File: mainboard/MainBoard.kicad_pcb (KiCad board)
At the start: 2 copper layers, 121.5 x 73.2 mm, 172 parts, among them J1 CONN_1x4, J10 CONN_2X2, J11 CONN_2X2, J17 HV, J18 CONN_1X2, J19 CONN_1X2, J2 CONN_2X3, J3 CONN_2X3, J4 CONN_2X2, J5 SWDEBUG_CONNECTOR, J6 CONN_2X2, J7 CONN_2X12, J8 CONN_1X2, J9 Micro_SD_Card_Det_Hirose_DM3AT, K1 KT12-1A, K2 G6DN 12V, Q1 SSM3K361TU,LF, Q2 TSM2312, SW1 RESET, U1 VX07805-1000, U10 DCDC_ISO_5V_ISO, U11 STM32G474, U12 M95256-WMN6P, U13 TS3704IPT, U14 CD4044, U15 CD4082, U16 ADCMP350, U17 CD74HC4067SM, U19 TCMT1103, U2 TPS2115A, U23 CD4072BPW, U24 LM358, U26 TCMT1103, U27 DCDC_ISO_5V, U28 MIC5365-3.3YC5, U29 Si8900, U3 ld1117s33, U30 MAX14878AWA+, U4 MainBoard_AD8244, U5 MCP2562, U6 LM358, U7 ADCMP354, U8 LTC6820, U9 HM2103

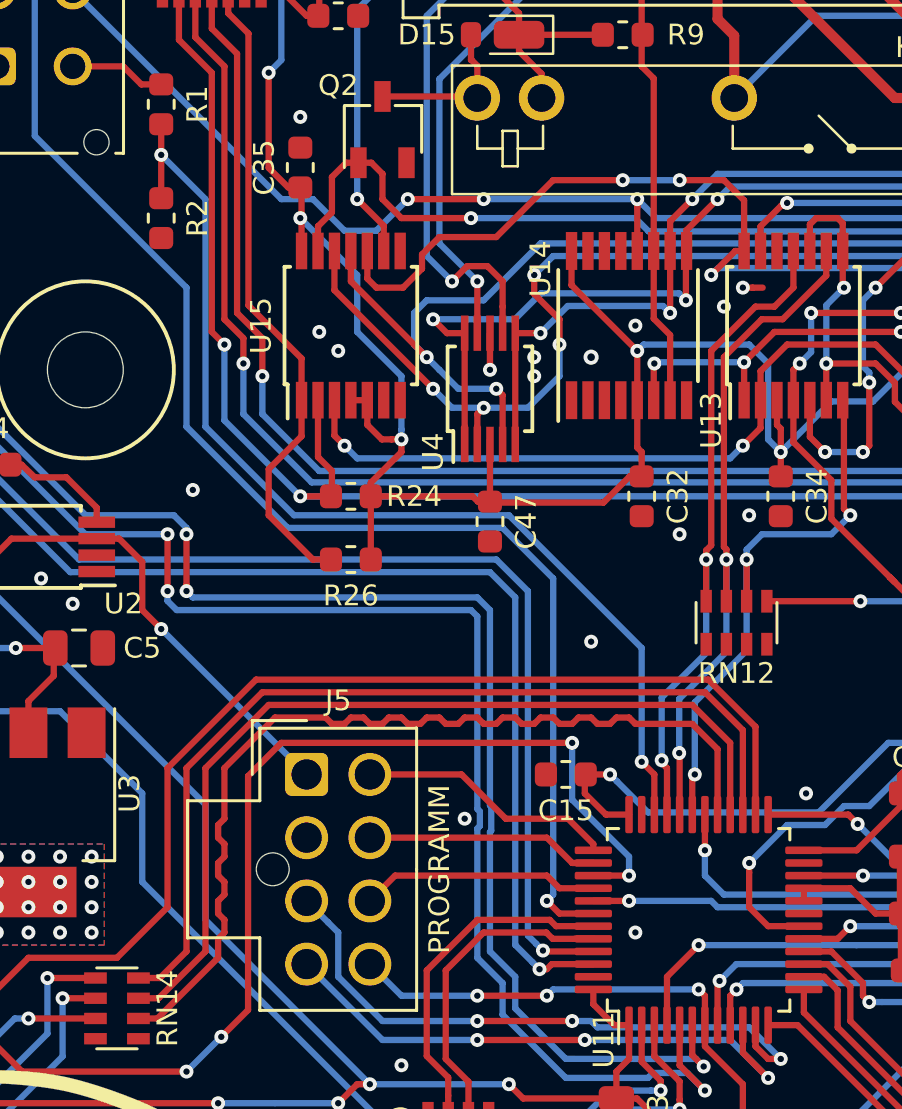
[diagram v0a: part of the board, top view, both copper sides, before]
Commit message: Corrected BOOT0
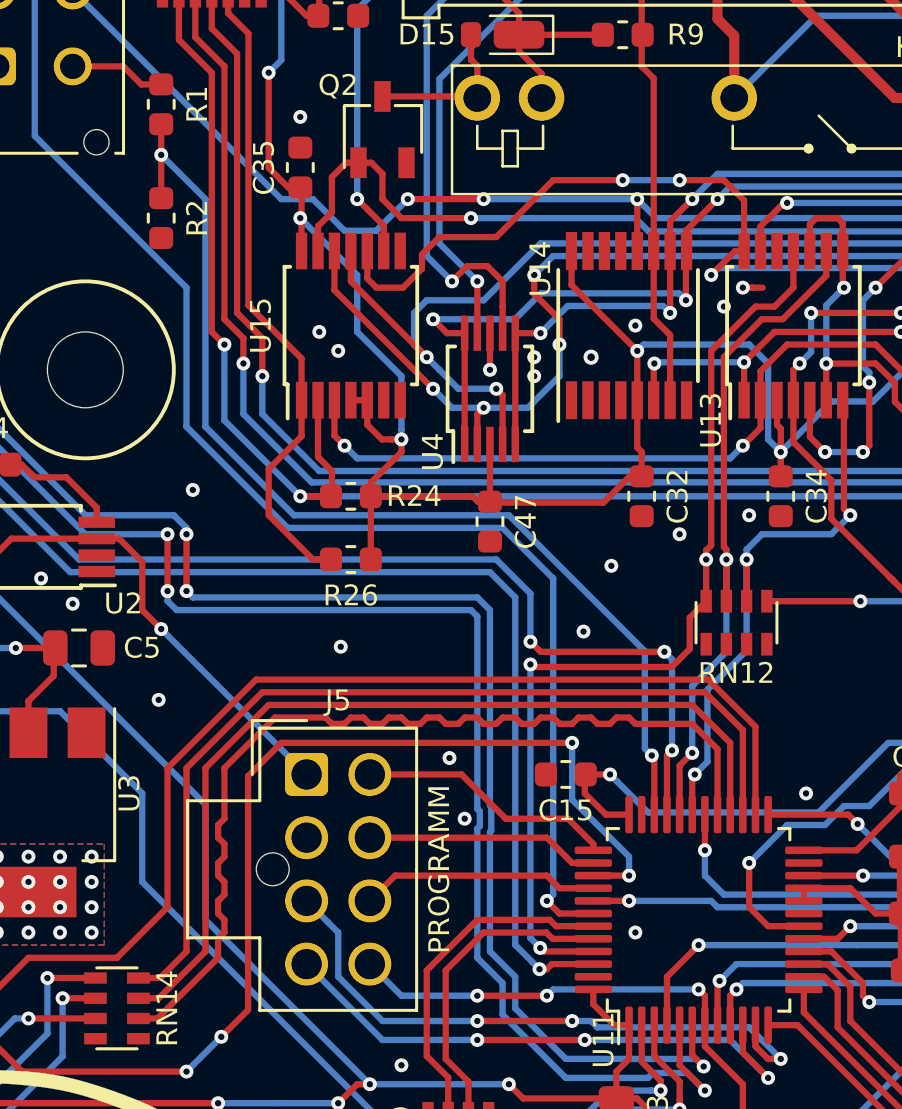
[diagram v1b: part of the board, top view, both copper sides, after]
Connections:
- RN10 pad 5: /AMS/A0 -> /AMS/A2
- RN10 pad 7: /AMS/A2 -> /AMS/A0
- U11 pad 33: /PC_ENDED -> /AMS/CAN_RX
- U11 pad 45: /AMS/CAN_RX -> /PC_ENDED
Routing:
- net /PC_ENDED: track 26.7 -> 38.0 mm, vias 2 -> 3
- net /AMS/CAN_RX: track 47.8 -> 45.5 mm, vias 2 -> 4
- net GND: vias 38 -> 42

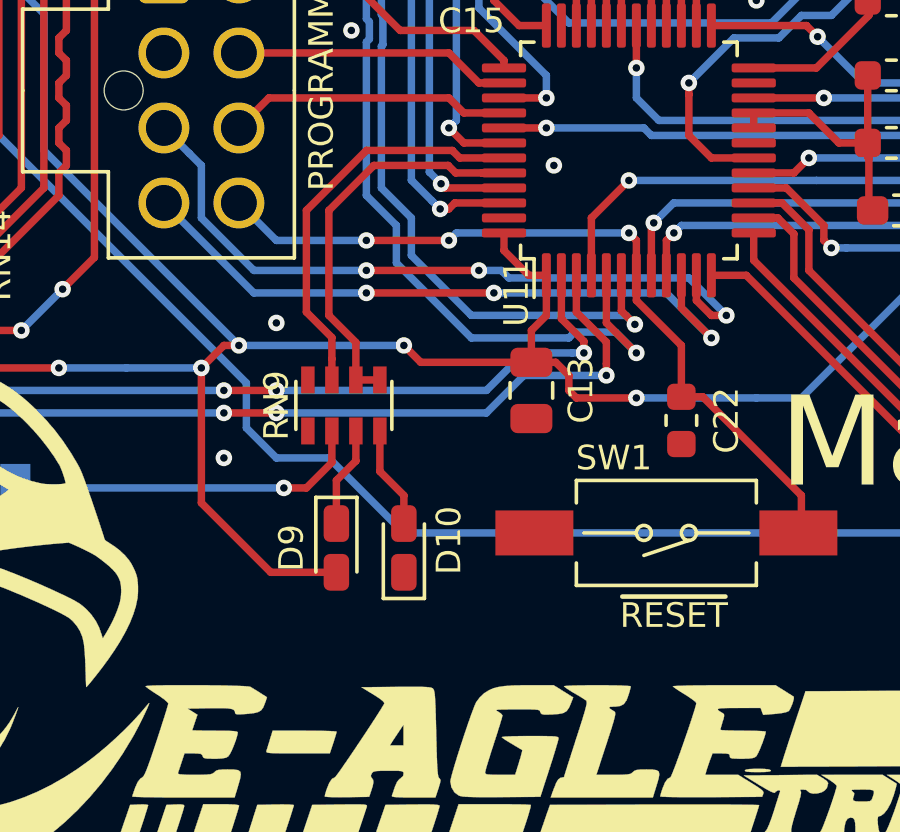
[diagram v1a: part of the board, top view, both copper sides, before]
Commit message: Added jumper for BOOT0 to 3V3
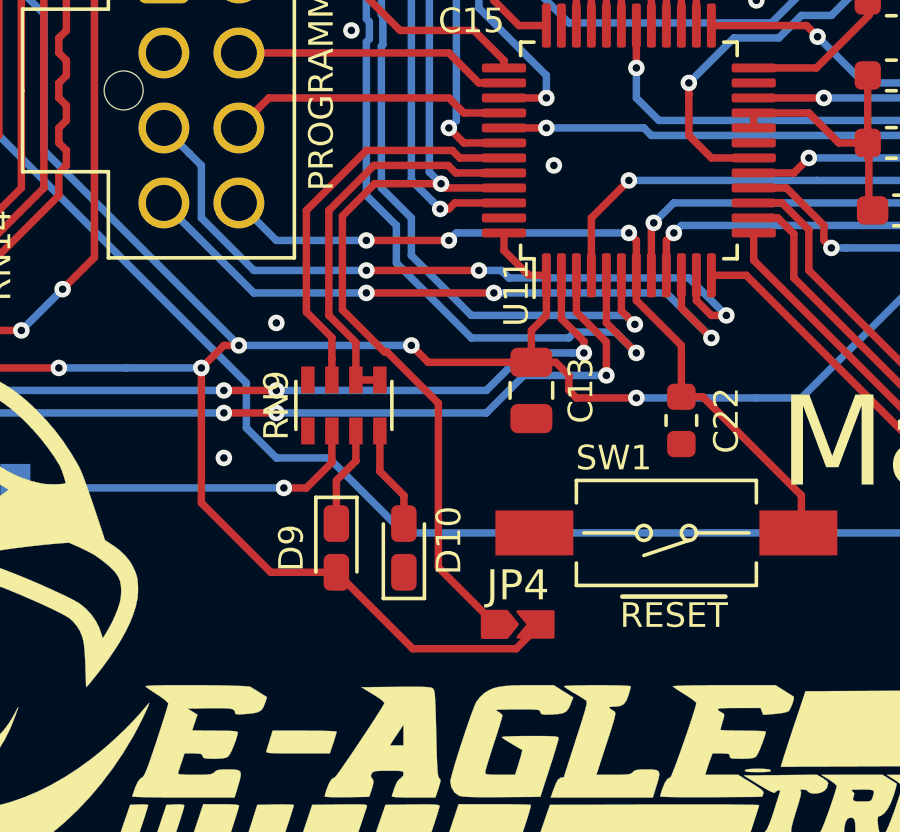
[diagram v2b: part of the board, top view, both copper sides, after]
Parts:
- added JP4: SolderJumper_2_Open, MainBoard:Jumper_SMD_0603, F.Cu at (68.5, 98.8)
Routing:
- net /PC_ENDED: track 38.0 -> 57.6 mm
- net +3V3: track 335.5 -> 343.7 mm

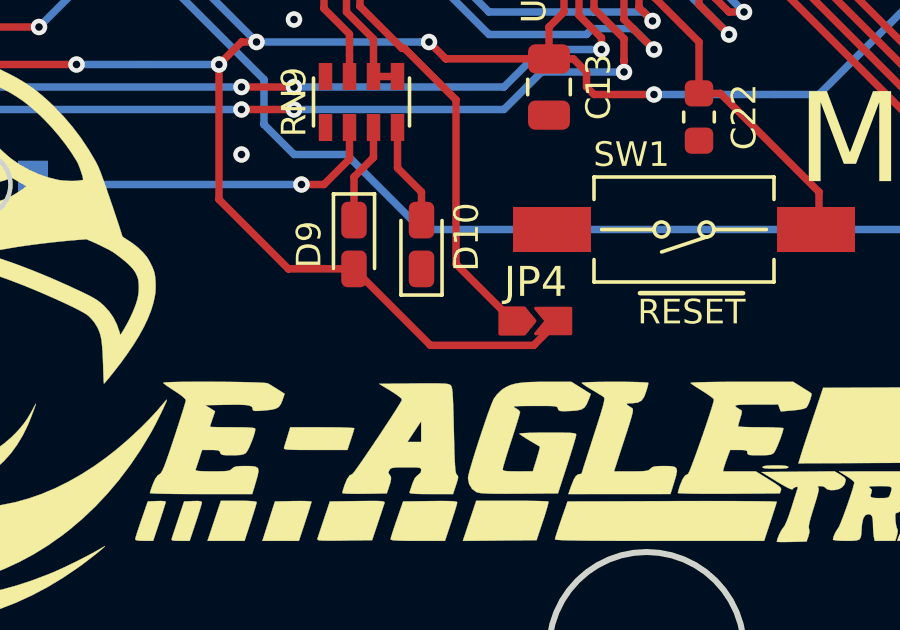
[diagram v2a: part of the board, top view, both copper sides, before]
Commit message: Added vias due to last boot0 modification
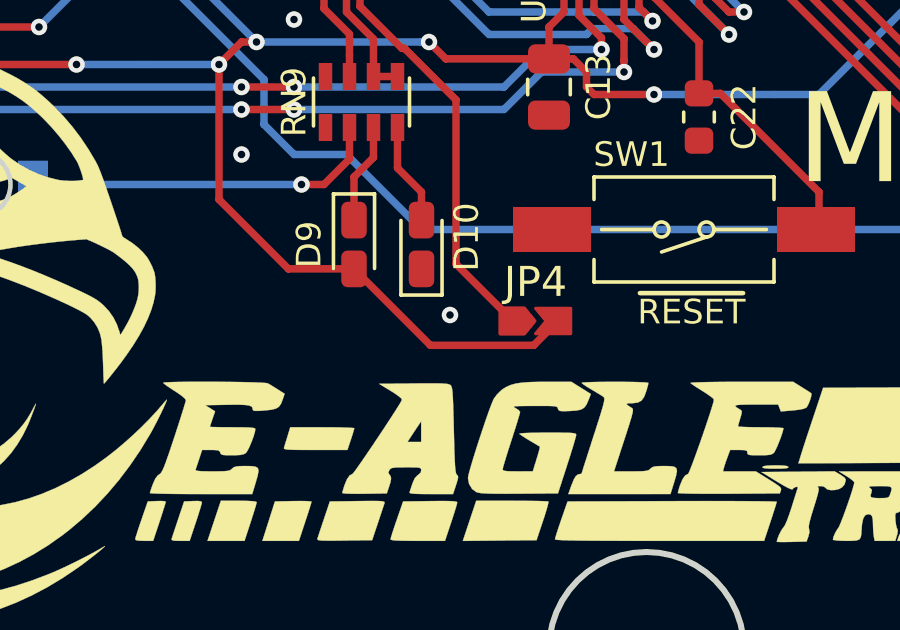
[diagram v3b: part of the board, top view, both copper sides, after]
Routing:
- net GND: vias 42 -> 43

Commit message: v1.1 as printed
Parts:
- removed C4, C5: 1uF, Capacitor_SMD:C_0805_2012Metric
- removed the G*** at (73.2, 103.5)
- removed the G*** at (44.8, 99.5)
- removed R38: 604, Resistor_SMD:R_0603_1608Metric
- removed R4: 470, Resistor_SMD:R_0603_1608Metric
- removed R69: 2K, Resistor_SMD:R_0603_1608Metric
- removed U10: DCDC_ISO_5V_ISO, MainBoard:DC_DC_ISO_ROExxxx
- removed U17: CD74HC4067SM, Package_SO:TSSOP-24_4.4x7.8mm_P0.65mm
- removed U23: CD4072BPW, Package_SO:TSSOP-14_4.4x5mm_P0.65mm
- removed U3: ld1117s33, Package_TO_SOT_SMD:SOT-223
- added B-H1: BOOT0, MainBoard:Jumper_SMD_0603, F.Cu at (131.8, 94.9)
- added C28: 1mF 16V, Capacitor_THT:CP_Radial_D10.0mm_P5.00mm, F.Cu at (167.0, 45.2)
- added C31: 100nF, Capacitor_SMD:C_0603_1608Metric, F.Cu at (187.0, 49.9)
- added C36: 1mF 16V, Capacitor_THT:CP_Radial_D10.0mm_P5.00mm, F.Cu at (167.0, 56.5)
- added C37: 100nF, Capacitor_SMD:C_0603_1608Metric, F.Cu at (187.0, 51.9)
- added C38: 20pF, Capacitor_SMD:C_0603_1608Metric, F.Cu at (164.3, 101.2)
- added C39: 20pF, Capacitor_SMD:C_0603_1608Metric, F.Cu at (164.2, 95.1)
- added C48: 100nF, Capacitor_SMD:C_0603_1608Metric, F.Cu at (157.7, 88.0)
- added D11: D, MainBoard:SOD_323HE, F.Cu at (196.1, 41.5)
- added D12: RGL34B, Diode_SMD:D_MiniMELF, F.Cu at (177.8, 45.2)
- added D13: DDZ13ASF 13V, Diode_SMD:D_SOD-323, F.Cu at (178.8, 41.3)
- added D16: D, MainBoard:SOD_323HE, F.Cu at (181.6, 55.1)
- added D17: D, MainBoard:SOD_323HE, F.Cu at (182.8, 46.5)
- added D18: RGL34B, Diode_SMD:D_MiniMELF, F.Cu at (177.8, 56.5)
- added D19: D, MainBoard:SOD_323HE, F.Cu at (218.1, 78.3)
- added D20: D, MainBoard:SOD_323HE, F.Cu at (218.1, 81.6)
- added D21: 1N4148W, Diode_SMD:D_SOD-123, F.Cu at (224.3, 100.0)
- added G***: LOGO, MainBoard:logo_21.2mm, F.Cu at (179.8, 102.2)
- added H5: MountingHole, MountingHole:MountingHole_3mm, F.Cu at (143.6, 56.0)
- added J12: SPARE_PINS, Connector_PinHeader_2.54mm:PinHeader_2x05_P2.54mm_Vertical, F.Cu at (154.2, 80.5)
- added JP1: prom_select, Jumper:SolderJumper-3_P1.3mm_Open_RoundedPad1.0x1.5mm, F.Cu at (213.7, 81.0)
- added JP2: 3V3_PROG, Jumper:SolderJumper-2_P1.3mm_Open_RoundedPad1.0x1.5mm, F.Cu at (122.5, 97.5)
- added JP5: AIR mode sel2, Jumper:SolderJumper-3_P1.3mm_Bridged12_RoundedPad1.0x1.5mm, F.Cu at (182.2, 62.1)
- added JP6: SolderJumper_3_Open, Jumper:SolderJumper-3_P1.3mm_Open_RoundedPad1.0x1.5mm, F.Cu at (230.2, 97.1)
- added JP7: SolderJumper_2_Open, Jumper:SolderJumper-2_P1.3mm_Open_RoundedPad1.0x1.5mm, F.Cu at (122.8, 50.0)
- added Q10: NTR5105PT1G, Package_TO_SOT_SMD:SOT-23, F.Cu at (131.7, 61.1)
- added Q11: NTR5105PT1G, Package_TO_SOT_SMD:SOT-23, F.Cu at (127.4, 61.1)
- added Q12: NTR5105PT1G, Package_TO_SOT_SMD:SOT-23, F.Cu at (123.1, 61.1)
- added Q3: DMN10H220L, Package_TO_SOT_SMD:SOT-23, F.Cu at (177.0, 51.4)
- added Q4: 2N7002NXAKR, Package_TO_SOT_SMD:SOT-23, F.Cu at (144.6, 65.7)
- added Q5: 2N7002NXAKR, Package_TO_SOT_SMD:SOT-23, F.Cu at (187.0, 60.8)
- added Q6: 2N7002NXAKR, Package_TO_SOT_SMD:SOT-23, F.Cu at (187.0, 46.8)
- added Q7: DMN10H220L, Package_TO_SOT_SMD:SOT-23, F.Cu at (177.0, 62.5)
- added Q8: NTR5105PT1G, Package_TO_SOT_SMD:SOT-23, F.Cu at (148.7, 65.7)
- added Q9: NTR5105PT1G, Package_TO_SOT_SMD:SOT-23, F.Cu at (152.7, 65.7)
- added R33: 0, Resistor_SMD:R_0603_1608Metric, F.Cu at (163.7, 48.1)
- added R36: 120, Resistor_SMD:R_0805_2012Metric, F.Cu at (209.0, 106.0)
- added R40: 0, Resistor_SMD:R_0603_1608Metric, F.Cu at (151.2, 70.1)
- added RN15: 100K, MainBoard:R_network_4x1_bourns_CAY16, F.Cu at (193.0, 50.9)
- added RN16: 330K, MainBoard:R_network_4x1_bourns_CAY16, F.Cu at (182.8, 50.9)
- added RN17: 100K, MainBoard:R_network_4x1_bourns_CAY16, F.Cu at (170.4, 79.8)
- added RN18: 100K, MainBoard:R_network_4x1_bourns_CAY16, F.Cu at (183.6, 91.2)
- added RN19: 22, MainBoard:R_network_4x1_bourns_CAY16, F.Cu at (191.4, 99.4)
- added RN20: 22, MainBoard:R_network_4x1_bourns_CAY16, F.Cu at (129.4, 65.8)
- added RN21: 22, MainBoard:R_network_4x1_bourns_CAY16, F.Cu at (148.7, 70.1)
- added RN22: 22, MainBoard:R_network_4x1_bourns_CAY16, F.Cu at (143.3, 100.8)
- added RV1: 10k, Potentiometer_SMD:Potentiometer_Bourns_3314J_Vertical, F.Cu at (226.1, 95.8)
- added SW2: SD_RESET, MainBoard:Button_SMD_6x3.5x4.3mm, F.Cu at (120.2, 79.5)
- added TP1: 3V3, TestPoint:TestPoint_Pad_D1.0mm, F.Cu at (125.6, 97.1)
- added TP10: TS_DIVIDER, TestPoint:TestPoint_Pad_D1.0mm, F.Cu at (223.8, 66.2)
- added TP11: 5VISO, TestPoint:TestPoint_Pad_D1.0mm, F.Cu at (216.2, 98.6)
- added TP12: TSV_FT, TestPoint:TestPoint_Pad_D1.0mm, F.Cu at (213.5, 88.8)
- added TP13: PackV_FT, TestPoint:TestPoint_Pad_D1.0mm, F.Cu at (213.5, 86.6)
- added TP14: 3V3ISO, TestPoint:TestPoint_Pad_D1.0mm, F.Cu at (216.3, 92.0)
- added TP15: Ip_high, TestPoint:TestPoint_Pad_D1.0mm, F.Cu at (106.0, 57.0)
- added TP16: BMS_FAULT, TestPoint:TestPoint_Pad_D1.0mm, F.Cu at (138.6, 83.9)
- added TP17: MUX_OUTPUT, TestPoint:TestPoint_Pad_D1.0mm, F.Cu at (155.8, 86.8)
- added TP18: TS_OVER_60V, TestPoint:TestPoint_Pad_D1.0mm, F.Cu at (194.1, 67.6)
- added TP19: PC_ST, TestPoint:TestPoint_Pad_D1.0mm, F.Cu at (134.2, 65.8)
- added TP2: 5V, TestPoint:TestPoint_Pad_D1.0mm, F.Cu at (116.0, 98.5)
- added TP20: AIR+_GATE, TestPoint:TestPoint_Pad_D1.0mm, F.Cu at (190.2, 48.0)
- added TP21: AIR-_GATE, TestPoint:TestPoint_Pad_D1.0mm, F.Cu at (190.2, 46.0)
- added TP22: AIR+_STATUS, TestPoint:TestPoint_Pad_D1.0mm, F.Cu at (163.2, 62.1)
- added TP23: AIR-_STATUS, TestPoint:TestPoint_Pad_D1.0mm, F.Cu at (161.4, 64.0)
- added TP24: SD_OK, TestPoint:TestPoint_Pad_D1.0mm, F.Cu at (136.3, 65.8)
- added TP25: BMS_LATCHED, TestPoint:TestPoint_Pad_D1.0mm, F.Cu at (125.0, 65.6)
- added TP26: IMD_LATCHED, TestPoint:TestPoint_Pad_D1.0mm, F.Cu at (125.0, 67.6)
- added TP27: TS_ON, TestPoint:TestPoint_Pad_D1.0mm, F.Cu at (140.7, 83.9)
- added TP28: TS_ON_12V, TestPoint:TestPoint_Pad_D1.0mm, F.Cu at (138.3, 65.8)
- added TP29: GND, MainBoard:TestPoint_GNDedge, F.Cu at (106.2, 110.8)
- added TP3: 12V, TestPoint:TestPoint_Pad_D1.0mm, F.Cu at (90.4, 85.1)
- added TP30: GND, MainBoard:TestPoint_GNDedge, F.Cu at (186.6, 39.7)
- added TP31: -BATT, MainBoard:TestPoint_GNDedge, F.Cu at (207.3, 110.8)
- added TP33: VCAP, TestPoint:TestPoint_Pad_D1.0mm, F.Cu at (150.5, 82.6)
- added TP35: IMD_PWM, TestPoint:TestPoint_Pad_D1.0mm, F.Cu at (114.4, 57.8)
- added TP38: VS_FT, TestPoint:TestPoint_Pad_D1.0mm, F.Cu at (213.5, 84.4)
- added TP4: FROM_SD, TestPoint:TestPoint_Pad_D1.0mm, F.Cu at (182.7, 70.0)
- added TP43: 11, TestPoint:TestPoint_Pad_D1.0mm, F.Cu at (196.1, 58.1)
- added TP44: 9, TestPoint:TestPoint_Pad_D1.0mm, F.Cu at (195.7, 60.2)
- added TP45: 13, TestPoint:TestPoint_Pad_D1.0mm, F.Cu at (196.3, 55.7)
- added TP46: 14, TestPoint:TestPoint_Pad_D1.0mm, F.Cu at (196.5, 53.5)
- added TP5: FROM_TSMS, TestPoint:TestPoint_Pad_D1.0mm, F.Cu at (182.7, 66.0)
- added TP6: TO_TSMS, TestPoint:TestPoint_Pad_D1.0mm, F.Cu at (182.7, 68.0)
- added TP7: BSPD_SIG, TestPoint:TestPoint_Pad_D1.0mm, F.Cu at (140.4, 65.9)
- added TP8: IMD_FAULT, TestPoint:TestPoint_Pad_D1.0mm, F.Cu at (116.9, 48.6)
- added TP9: Ip_low, TestPoint:TestPoint_Pad_D1.0mm, F.Cu at (106.0, 55.1)
- added Y1: 26MHz, Crystal:Crystal_SMD_3225-4Pin_3.2x2.5mm, F.Cu at (164.3, 98.2)
- C1: value 22uF -> 100nF; footprint Capacitor_SMD:C_1206_3216Metric -> Capacitor_SMD:C_0603_1608Metric
- C19, C21: value 100nF -> 1uF; footprint Capacitor_SMD:C_0603_1608Metric -> Capacitor_SMD:C_0805_2012Metric
- C2: value 10uF -> 100nF; footprint Capacitor_SMD:C_0805_2012Metric -> Capacitor_SMD:C_0603_1608Metric
- C25: footprint Capacitor_SMD:C_0603_1608Metric -> Capacitor_SMD:C_0805_2012Metric
- C3: value 1uF -> 100nF; footprint Capacitor_SMD:C_0805_2012Metric -> Capacitor_SMD:C_0603_1608Metric
- C42: value 6.8uF -> 10uF
- D14: value 12V -> DDZ13ASF 13V
- D5, D6, D7: value 3V -> DDZ3V3ASF 3V3
- J10: value CONN_2X2 -> AIR+
- J4: footprint MainBoard:Molex_Micro-Fit_3.0_43045-0412_2x02_P3.00mm_Vertical -> MainBoard:Molex_Micro-Fit_3.0_43045-0612_2x03_P3.00mm_Vertical
- J5: footprint MainBoard:Molex_Nano-Fit_105310-xx08_2x04_P2.50mm_Vertical -> Connector_Molex:Molex_Nano-Fit_105310-xx10_2x05_P2.50mm_Vertical
- J6: value CONN_2X2 -> AIR-
- J9: footprint MainBoard:MicroSD_Hirose_DM3AT-SF-PEJM5 -> Connector_Card:microSD_HC_Hirose_DM3AT-SF-PEJM5
- JP3: footprint MainBoard:Jumper_SMD_0603 -> Jumper:SolderJumper-2_P1.3mm_Open_RoundedPad1.0x1.5mm
- JP4: value SolderJumper_2_Open -> AIR mode sel1; footprint MainBoard:Jumper_SMD_0603 -> Jumper:SolderJumper-3_P1.3mm_Bridged12_RoundedPad1.0x1.5mm
- Q1: value SSM3K361TU,LF -> NTR5105PT1G; footprint Package_TO_SOT_SMD:SOT-323_SC-70 -> Package_TO_SOT_SMD:SOT-23
- Q2: value TSM2312 -> DMN10H220L; footprint Package_TO_SOT_SMD:TSOT-23 -> Package_TO_SOT_SMD:SOT-23
- R13: value 330K -> 1M
- R16: value 1M -> 1K
- R19: value 2K -> 1K
- R20: value 2K -> 0
- R30: value 100K -> 0
- R31, R32: value 22 -> 0
- R34: value 150 -> 0
- R35: value 150 -> 120; footprint Resistor_SMD:R_0603_1608Metric -> Resistor_SMD:R_0805_2012Metric
- R39: value 1K4 -> 0
- R56, R64, R66: footprint Resistor_SMD:R_1206_3216Metric -> Resistor_SMD:R_2010_5025Metric
- R59: value 1K -> 100
- R6: value 120 -> 10K; footprint Resistor_SMD:R_0805_2012Metric -> Resistor_SMD:R_0603_1608Metric
- RN1: value 1K -> 100K
- RN5: value 100K -> 330K
- U1: value VX07805-1000 -> Tex_DCDC; footprint MainBoard:DC_DC_VXO7805_1000 -> MainBoard:Tex_DCDC_vertical
- U11: value STM32G474 -> TS3704IPT; footprint Package_QFP:LQFP-48_7x7mm_P0.5mm -> Package_SO:TSSOP-14_4.4x5mm_P0.65mm
- U2: value TPS2115A -> TSC211; footprint Package_SO:TSSOP-8_4.4x3mm_P0.65mm -> Package_TO_SOT_SMD:SOT-363_SC-70-6
- U30: footprint Package_SO:SOIC-8_7.5x5.85mm_P1.27mm -> Package_SO:SOIC-8W_5.3x5.3mm_P1.27mm
- U4: moved to B.Cu
- U8: value LTC6820 -> CD74HC4067SM; footprint MainBoard:MSOP-16 -> Package_SO:TSSOP-24_4.4x7.8mm_P0.65mm
- U9: value HM2103 -> STM32F446RE_64PIN; footprint MainBoard:HM2103 -> Package_QFP:LQFP-64_10x10mm_P0.5mm
- moved C1 201.1 mm to (225.2, 101.8), turned to 180 degrees
- moved C2 192.3 mm to (225.2, 103.5), turned to 0 degrees
- moved U2 186.0 mm to (228.2, 102.8), turned to 0 degrees
- moved R19 180.4 mm to (209.9, 77.5)
- moved R3 176.9 mm to (215.3, 84.4), turned to 0 degrees
- moved C3 169.2 mm to (211.8, 84.4), turned to 180 degrees
- moved R24 138.0 mm to (196.5, 68.8), turned to 270 degrees
- moved D8 134.8 mm to (184.8, 97.1), turned to 180 degrees
- moved U11 121.2 mm to (190.4, 56.3), turned to 0 degrees
- moved JP4 120.3 mm to (182.2, 59.4), turned to 0 degrees
- moved R16 112.2 mm to (211.5, 77.5), turned to 270 degrees
- moved J8 109.8 mm to (232.1, 104.6)
- moved C29 105.5 mm to (190.7, 59.9), turned to 0 degrees
- moved J19 100.0 mm to (239.1, 93.1), turned to 90 degrees
- moved J18 99.9 mm to (239.2, 104.7), turned to 90 degrees
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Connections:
- net /HV/5V_FROM_CELL renamed Net-(C17-Pad1)
- net /Shutdown/dissipation renamed /AIRs/dissipation
- C1 pad 1: +12V -> /HV/0V5ref
- C1 pad 2: GND -> -BATT
- C18 pad 1: +5V -> +3V3
- C19 pad 1: GND -> Net-(C19-Pad1)
- C19 pad 2: Net-(C19-Pad2) -> GND
- C2 pad 1: /5V_FROM_12V -> -BATT
- C2 pad 2: GND -> /HV/3V3ISO
- C21 pad 1: +3V3 -> Net-(C19-Pad1)
- C29 pad 1: +3V3 -> +12V
- C3 pad 1: /5V_USB -> -BATT
- C3 pad 2: GND -> /HV/VS_FT
- F2 pad 1: Net-(C5-Pad1) -> /3V3_prefuse
- J10 pad 1: /FROM_TSMS -> /AIRs/AIR+_STATUS
- J10 pad 2: /Shutdown/LAST_AIR -> +12V
- J10 pad 3: /FB_AIR+ -> Net-(J10-Pad3)
- J10 pad 4: +12V -> Net-(C36-Pad1)
- J11 pad 1: /IM -> /HV/ISO_CANL
- J11 pad 2: /IP -> /HV/ISO_CANH
- J3 pad 5: /IMD_Fault -> /IMD_FAULT
- J4 pad 1: /HV/EXT_GND -> /HV/PROMINENT-
- J4 pad 2: /HV/PROMINENT- -> /HV/PROMINENT+
- J4 pad 3: /HV/EXT_5V -> /HV/JUMPER_CELLBOARD
- J4 pad 4: /HV/PROMINENT+ -> /HV/CELLBOARD_5V
- J5 pad 1: /5V_USB -> GND
- J5 pad 2: GND -> /SWCLK_MCU
- J5 pad 3: /RX_MCU -> /SWDIO_MCU
- J5 pad 4: /TX_MCU -> Net-(J5-Pad4)
- J5 pad 5: /SWDIO_MCU -> /TX_MCU
- J5 pad 6: /SWCLK_MCU -> GND
- J5 pad 7: /SWO_MCU -> /NRST_MCU
- J5 pad 8: /NRST_MCU -> /SWO_MCU
- J6 pad 1: +12V -> /AIRs/AIR-_STATUS
- J6 pad 2: /FB_AIR- -> +12V
- J6 pad 3: GND -> Net-(J6-Pad3)
- J6 pad 4: /FROM_TSMS -> Net-(C28-Pad1)
- J7 pad 7: /LED_INDICATOR -> /TSAL
- J8 pad 1: /IP -> /HV/VS-
- J8 pad 2: /IM -> /HV/VS+
- JP4 pad 1: +3V3 -> Net-(D16-Pad1)
- JP4 pad 2: /PC_ENDED -> Net-(JP4-Pad2)
- Q1 pad 1: /FB_PC_END -> Net-(Q1-Pad1)
- Q1 pad 2: GND -> +12V
- Q1 pad 3: /Shutdown/LAST_AIR -> Net-(Q1-Pad3)
- Q2 pad 1: /FB_SD_MINIRELAY -> Net-(Q2-Pad1)
- R1 pad 2: /IMD -> /IMD_PWM
- R13 pad 1: +3V3 -> Net-(D5-Pad1)
- R13 pad 2: /AMS/MISO -> /FROM_SD
- R14 pad 1: Net-(D5-Pad1) -> Net-(D6-Pad1)
- R14 pad 2: /FROM_SD -> /TO_TSMS
- R15 pad 1: Net-(D6-Pad1) -> Net-(D7-Pad1)
- R15 pad 2: /TO_TSMS -> /FROM_TSMS
- R16 pad 1: Net-(D7-Pad1) -> Net-(R16-Pad1)
- R16 pad 2: /FROM_TSMS -> /HV/3V3ISO
- R19 pad 1: +3V3 -> /HV/~RST~_8902
- R19 pad 2: /AMS/~W~ -> Net-(R16-Pad1)
- R2 pad 1: /IMD -> /IMD_PWM
- R20 pad 1: +3V3 -> Net-(D4-Pad1)
- R20 pad 2: /AMS/MISO_2 -> /TSAL
- R24 pad 2: /FB_TS_OVER_60V -> /Probing/FB_OVER_60V_12V
- R25 pad 1: /BSPD_SIG -> GND
- R25 pad 2: GND -> /BSPD_SIG
- R27 pad 1: GND -> Net-(D4-Pad2)
- R27 pad 2: Net-(D4-Pad1) -> +12V
- R3 pad 1: /5V_USB -> /HV/VS_FT
- R3 pad 2: GND -> /HV/VS
- R30 pad 1: /AMS/CHECK_MUX -> /FROM_TSMS
- R30 pad 2: +3V3 -> Net-(C36-Pad1)
- R31 pad 1: /AMS/ADC_TX -> /FROM_TSMS
- R31 pad 2: Net-(R31-Pad2) -> Net-(C28-Pad1)
- R32 pad 1: /AMS/ADC_RX -> GND
- R32 pad 2: Net-(R32-Pad2) -> Net-(J10-Pad3)
- R34 pad 1: /AMS/IP_LV -> Net-(Q1-Pad3)
- R34 pad 2: Net-(C19-Pad2) -> /TSAL
- R35 pad 1: Net-(C19-Pad2) -> /CAN+
- R35 pad 2: /AMS/IM_LV -> /CAN-
- R39 pad 1: GND -> /Shutdown/EN_BMS_SD
- R39 pad 2: /AMS/ICMP -> /Shutdown/BMS_LATCHED
- R6 pad 1: /IP -> +3V3
- R6 pad 2: /IM -> /AMS/SPI2_MISO
- RN1 pad 2: Net-(RN1-Pad2) -> +3V3
- RN1 pad 7: Net-(RN1-Pad7) -> /AMS/~W~
- RN10 pad 5: /AMS/A2 -> /Probing/FB_AIR+_GATE
- RN10 pad 6: /AMS/A1 -> /Probing/FB_AIR-
- RN10 pad 7: /AMS/A0 -> /Probing/FB_AIR+
- RN10 pad 8: /AMS/A3 -> /Probing/FB_LATCH_BMS
- RN11 pad 1: /AMS/FB_PC_END_12V -> GND
- RN11 pad 2: /AMS/FB_AIR- -> GND
- RN11 pad 3: /AMS/FB_AIR+ -> GND
- RN11 pad 4: /AMS/FB_TSAL_OVER60V -> GND
- RN11 pad 5: GND -> /Probing/FB_LATCH_IMD
- RN11 pad 6: GND -> /Probing/FB_BMS_SD
- RN11 pad 7: GND -> /Probing/FB_IMD_SD
- RN11 pad 8: GND -> /Probing/FB_BMS_12V
- RN12 pad 5: /PC_ENDED -> /AMS/BOOT0
- RN12 pad 6: /TS_ON -> /AMS/TS_ON
- RN12 pad 7: /BMS_Fault -> /AMS/BMS_FAULT
- RN14 pad 1: /AMS/SPI2_SCK -> Net-(RN14-Pad1)
- RN14 pad 2: /AMS/SPI2_MISO -> /AMS/SPI2_MOSI
- RN14 pad 3: /AMS/SPI2_MOSI -> /AMS/SPI2_SCK
- RN14 pad 4: Net-(RN14-Pad4) -> /AMS/SPI2_MISO
- RN14 pad 5: Net-(RN14-Pad5) -> /AMS/MISO_2
- RN14 pad 6: /AMS/MOSI_2 -> /AMS/SCK_2
- RN14 pad 7: /AMS/MISO_2 -> /AMS/MOSI_2
- RN14 pad 8: /AMS/SCK_2 -> Net-(RN14-Pad8)
- RN2 pad 1: /FB_BMS -> /AIRs/AIR-_GATE
- RN2 pad 2: /IMD_Fault -> +3V3
- RN2 pad 3: /FB_LACTH_BMS -> /Probing/FB_RELAY_LV_12V
- RN2 pad 4: /FB_LACTH_IMD -> /IMD_FAULT
- RN2 pad 5: /AMS/FB_LATCH_IMD -> /AMS/FB_IMD_FAULT
- RN2 pad 6: /AMS/FB_LATCH_BMS -> /AMS/FB_RELAY_LV
- RN2 pad 7: /AMS/FB_IMD_FAULT -> /Probing/CHECK_MUX
- RN2 pad 8: /AMS/FB_BMS_12V -> /Probing/FB_AIR-_GATE
- RN3 pad 1: /FB_TS_ON -> /AIRs/AIR+_GATE
- RN3 pad 2: /FB_BMS_SD -> /TSAL
- RN3 pad 3: /FB_IMD_SD -> /Shutdown/BMS_LATCHED
- RN3 pad 4: /FB_SD_MINIRELAY -> /Probing/FB_LATCH_IMD_12V
- RN3 pad 5: /AMS/FB_RELAY_LV -> /Probing/FB_LATCH_BMS
- RN3 pad 6: /AMS/FB_IMD_SD -> /Probing/FB_AIR+
- RN3 pad 7: /AMS/FB_BMS_SD -> /Probing/FB_AIR-
- RN3 pad 8: /AMS/FB_TS_ON_12V -> /Probing/FB_AIR+_GATE
- RN4 pad 1: /FB_PC_END -> /Probing/FB_TS_ON_TO_12V
- RN4 pad 2: /FB_AIR- -> /Shutdown/EN_BMS_SD
- RN4 pad 3: /FB_AIR+ -> /Shutdown/EN_IMD_SD
- RN4 pad 4: /FB_TS_OVER_60V -> /Shutdown/BMS_FAULT_12V
- RN4 pad 5: /AMS/FB_TSAL_OVER60V -> /Probing/FB_BMS_12V
- RN4 pad 6: /AMS/FB_AIR+ -> /Probing/FB_IMD_SD
- RN4 pad 7: /AMS/FB_AIR- -> /Probing/FB_BMS_SD
- RN4 pad 8: /AMS/FB_PC_END_12V -> /Probing/FB_LATCH_IMD
- RN5 pad 1: /AMS/FB_BMS_12V -> /BSPD_SIG
- RN5 pad 2: /AMS/FB_IMD_FAULT -> /AIRs/AIR-_STATUS
- RN5 pad 3: /AMS/FB_LATCH_BMS -> /AIRs/AIR+_STATUS
- RN5 pad 4: /AMS/FB_LATCH_IMD -> /Probing/FB_OVER_60V_12V
- RN5 pad 5: GND -> /Probing/FB_TSAL_OVER60V
- RN5 pad 6: GND -> /Probing/FB_TSAL
- RN5 pad 7: GND -> /Probing/FB_BSPD_SIG
- RN5 pad 8: GND -> /Probing/FB_TS_ON_12V
- RN6 pad 1: /AMS/FB_TS_ON_12V -> Net-(RN6-Pad1)
- RN6 pad 2: /AMS/FB_BMS_SD -> /AMS/FB_FROM_TSMS
- RN6 pad 3: /AMS/FB_IMD_SD -> /Probing/FB_TO_TSMS
- RN6 pad 4: /AMS/FB_RELAY_LV -> /Probing/FB_FROM_SD
- RN6 pad 5: GND -> Net-(D5-Pad1)
- RN6 pad 6: GND -> Net-(D6-Pad1)
- RN6 pad 7: GND -> Net-(D7-Pad1)
- RN6 pad 8: GND -> Net-(RN6-Pad8)
- RN7 pad 1: Net-(D5-Pad1) -> GND
- RN7 pad 2: Net-(D6-Pad1) -> GND
- RN7 pad 3: Net-(D7-Pad1) -> GND
- RN7 pad 4: Net-(RN7-Pad4) -> GND
- RN7 pad 5: Net-(RN7-Pad5) -> /Probing/FB_AIR-_GATE
- RN7 pad 6: /AMS/FB_FROM_TSMS -> /Probing/CHECK_MUX
- RN7 pad 7: /AMS/FB_TO_TSMS -> /AMS/FB_RELAY_LV
- RN7 pad 8: /AMS/FB_FROM_SD -> /AMS/FB_IMD_FAULT
- RN8 pad 2: /LED_INDICATOR -> /TSAL
- RN8 pad 5: +12V -> GND
- RN8 pad 6: +12V -> GND
- RN8 pad 7: +12V -> GND
- U1 pad 1: +12V -> /3V3_prefuse
- U1 pad 3: /5V_FROM_12V -> Net-(F1-Pad2)
- U11 pad 1: +3V3 -> /AIRs/AIR-_GATE
- U11 pad 10: /TX_MCU -> +3V3
- U11 pad 11: /RX_MCU -> Net-(TP43-Pad1)
- U11 pad 12: /AMS/CS_6820 -> GND
- U11 pad 13: /AMS/SCK -> Net-(TP45-Pad1)
- U11 pad 14: /AMS/MISO -> Net-(TP46-Pad1)
- U11 pad 2: /AMS/CS_EEPROM -> /AIRs/AIR+_GATE
- U11 pad 3: /AMS/CARD_OK -> +12V
- U11 pad 4: /AMS/A1 -> Net-(JP5-Pad2)
- U11 pad 5: /AMS/Ip_low -> Net-(C37-Pad1)
- U11 pad 6: /AMS/Ip_high -> +3V3
- U11 pad 7: /NRST_MCU -> Net-(C31-Pad1)
- U11 pad 8: /AMS/A0 -> +3V3
- U11 pad 9: /AMS/A3 -> Net-(TP44-Pad1)
- U13 pad 1: /FB_BMS -> /Shutdown/BMS_FAULT_12V
- U13 pad 11: /PC_ENDED -> Net-(U13-Pad11)
- U13 pad 13: /FB_PC_END -> Net-(U13-Pad13)
- U13 pad 14: /FB_TS_ON -> /Probing/FB_TS_ON_TO_12V
- U13 pad 7: /BMS_Fault -> /AMS/BMS_FAULT
- U13 pad 9: /TS_ON -> /AMS/TS_ON
- U14 pad 10: /FB_LACTH_IMD -> /Probing/FB_LATCH_IMD_12V
- U14 pad 12: /IMD_Fault -> /IMD_FAULT
- U14 pad 6: /FB_BMS -> /Shutdown/BMS_FAULT_12V
- U14 pad 9: /FB_LACTH_BMS -> /Shutdown/BMS_LATCHED
- U15 pad 10: /FB_TS_ON -> /Probing/FB_TS_ON_TO_12V
- U15 pad 11: /FB_IMD_SD -> /Shutdown/EN_IMD_SD
- U15 pad 12: /FB_BMS_SD -> /Shutdown/EN_BMS_SD
- U15 pad 13: /FB_SD_MINIRELAY -> /Probing/FB_RELAY_LV_12V
- U15 pad 2: /FB_TS_OVER_60V -> /Probing/FB_OVER_60V_12V
- U19 pad 4: /FB_TS_OVER_60V -> /Probing/FB_OVER_60V_12V
- U2 pad 1: Net-(U2-Pad1) -> /HV/0V5ref
- U2 pad 2: GND -> -BATT
- U2 pad 3: /5V_USB -> /HV/3V3ISO
- U2 pad 4: Net-(R4-Pad2) -> /HV/VS+
- U2 pad 5: GND -> /HV/VS-
- U2 pad 6: /5V_FROM_12V -> /HV/VS
- U29 pad 12: Net-(R32-Pad2) -> Net-(RN19-Pad1)
- U29 pad 13: Net-(R31-Pad2) -> Net-(RN19-Pad2)
- U29 pad 5: Net-(U29-Pad5) -> /HV/VS_FT
- U30 pad 1: /AMS/ISO_CAN_RX -> Net-(RN19-Pad3)
- U30 pad 2: /AMS/ISO_CAN_TX -> Net-(RN19-Pad4)
- U30 pad 6: /IM -> /HV/ISO_CANL
- U30 pad 7: /IP -> /HV/ISO_CANH
- U4 pad 1: /FB_LACTH_BMS -> /Shutdown/BMS_LATCHED
- U4 pad 10: /FB_LACTH_BMS -> /Shutdown/BMS_LATCHED
- U4 pad 2: /FB_BMS_SD -> /Shutdown/EN_BMS_SD
- U4 pad 4: /FB_IMD_SD -> /Shutdown/EN_IMD_SD
- U4 pad 5: /FB_LACTH_IMD -> /Probing/FB_LATCH_IMD_12V
- U4 pad 6: /FB_LACTH_IMD -> /Probing/FB_LATCH_IMD_12V
- U5 pad 1: /AMS/CAN_TX -> Net-(RN22-Pad3)
- U5 pad 4: /AMS/CAN_RX -> Net-(RN22-Pad4)
- U8 pad 1: GND -> /AMS/MUX_OUTPUT
- U8 pad 10: /AMS/IM_LV -> /AMS/MUX_A0
- U8 pad 11: /AMS/IP_LV -> /AMS/MUX_A1
- U8 pad 12: +5V -> GND
- U8 pad 13: GND -> /AMS/MUX_A3
- U8 pad 14: GND -> /AMS/MUX_A2
- U8 pad 15: /AMS/ICMP -> GND
- U8 pad 16: /AMS/IBIAS -> /Probing/FB_TO_TSMS
- U8 pad 2: /AMS/MOSI -> /Probing/FB_BMS_12V
- U8 pad 3: /AMS/MISO -> /Probing/FB_IMD_SD
- U8 pad 4: /AMS/SCK -> /Probing/FB_BMS_SD
- U8 pad 5: /AMS/CS_6820 -> /Probing/FB_LATCH_IMD
- U8 pad 6: +3V3 -> /Probing/FB_TSAL_OVER60V
- U8 pad 7: GND -> /Probing/FB_TSAL
- U8 pad 8: GND -> /Probing/FB_BSPD_SIG
- U8 pad 9: +5V -> /Probing/FB_TS_ON_12V
- U9 pad 1: /IM -> +3V3
- U9 pad 2: Net-(U9-Pad2) -> /AMS/PC13
- U9 pad 3: /IP -> Net-(U9-Pad3)
- U9 pad 4: /AMS/IP_LV -> Net-(U9-Pad4)
- U9 pad 6: /AMS/IM_LV -> Net-(C39-Pad1)
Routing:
- net +12V: track 197.3 -> 449.1 mm, vias 12 -> 14
- net GND: track 15.4 -> 187.9 mm, vias 43 -> 149
- net Net-(JP5-Pad3): track 0.00 -> 122.7 mm, vias 0 -> 6
- net Net-(Q6-Pad1): track 0.00 -> 122.0 mm, vias 0 -> 6
- net /Probing/FB_OVER_60V_12V: track 0.00 -> 111.4 mm, vias 0 -> 6
- net /IMD_FAULT: track 0.00 -> 99.4 mm, vias 0 -> 4
- net /FB_TS_OVER_60V: track 98.1 -> 0.00 mm, vias 4 -> 0
- net +3V3: track 343.7 -> 439.8 mm, vias 28 -> 22
- net /FB_AIR-: track 90.7 -> 0.00 mm, vias 4 -> 0
- net /TSAL: track 0.00 -> 84.8 mm, vias 0 -> 7
- net /FB_AIR+: track 78.8 -> 0.00 mm, vias 2 -> 0
- net /Shutdown/BMS_LATCHED: track 0.00 -> 75.2 mm, vias 0 -> 5
- net /Shutdown/BMS_FAULT_12V: track 0.00 -> 73.5 mm, vias 0 -> 6
- net /AIRs/AIR-_STATUS: track 0.00 -> 72.1 mm, vias 0 -> 4
- net /Probing/FB_LATCH_IMD_12V: track 0.00 -> 71.2 mm, vias 0 -> 9
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- added copper zone on F.Cu, net /AIRs/dissipation
- removed copper zone on B.Cu, net /dissipation
- removed copper zone on F.Cu, net /dissipation
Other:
- board size 121.5 x 73.2 mm -> 155 x 73.2 mm
- rule trace_min: 0.2 -> 0.25
- board text added: "5V_IN"
- board text added: "BSPD"
- board text added: "Fenice BMS - MainBoard V1.1"
- board text added: "PROGRAMMING"
- board text added: "PROMINET"
- board text added: "SHUNT"
- board text added: "TO_CELLS"
- board text added: "VS"
- board text added: "~RST~"
- board text removed: "*5V"
- board text removed: "5V+PROMINET"
- board text removed: "IM/CANL"
- board text removed: "IP/CANH"
- board text removed: "Mainboard_V1.0.5"
- board text removed: "PROGRAMM"
- board text removed: "RST"
- board text removed: "TO_BATT"

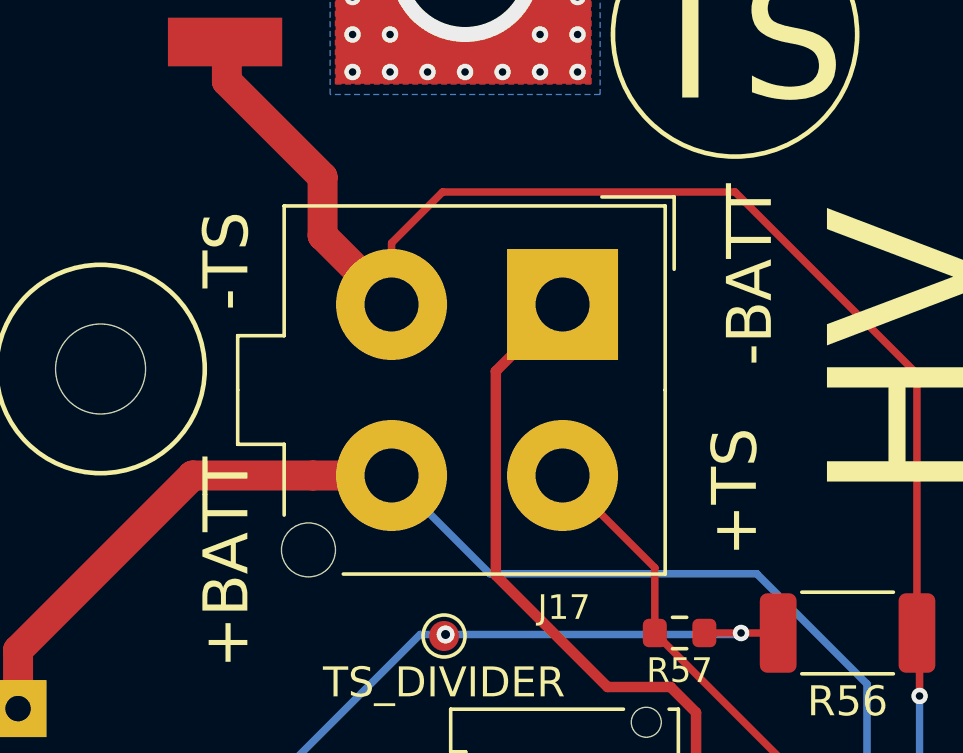
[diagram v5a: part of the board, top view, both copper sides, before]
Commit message: Renamed handcart detection
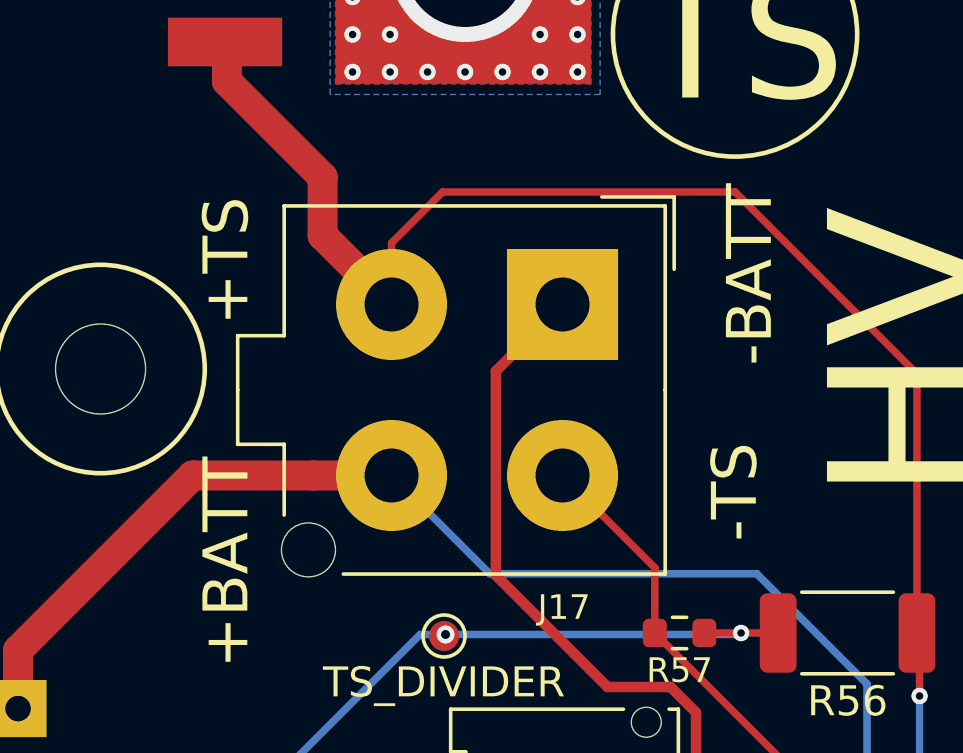
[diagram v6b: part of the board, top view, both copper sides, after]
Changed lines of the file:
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@@
     (effects (font (size 0.82 0.82) (thickness 0.153)) (justify mirror))
   )
-  (gr_text -TS (at 216.55 53.65 90) (layer F.SilkS)
+  (gr_text +TS (at 216.55 53.65 90) (layer F.SilkS)
     (effects (font (size 1.5 1.5) (thickness 0.375)))
   )
@@
     (effects (font (size 1.5 1.5) (thickness 0.375)))
   )
-  (gr_text +TS (at 233.5 61.35 90) (layer F.SilkS)
+  (gr_text -TS (at 233.5 61.35 90) (layer F.SilkS)
     (effects (font (size 1.5 1.5) (thickness 0.375)))
   )
